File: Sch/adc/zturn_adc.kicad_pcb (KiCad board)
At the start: 4 copper layers, 86 x 75.8 mm, 115 parts, among them CN1 SMA, CN2 SMA, CN3 AudioJack, J1 JP2, J3 JP2, J4 JP2, P1 CONN_02X40, T1 ETC1-1-13, U1 LTC2292, U2 LP5907_SOT-23, U3 LP5907_SOT-23, U4 NC7SVU04-SC70, U5 NC7SVU04-SC70, U6 NAU8822LYG, X1 TCXO

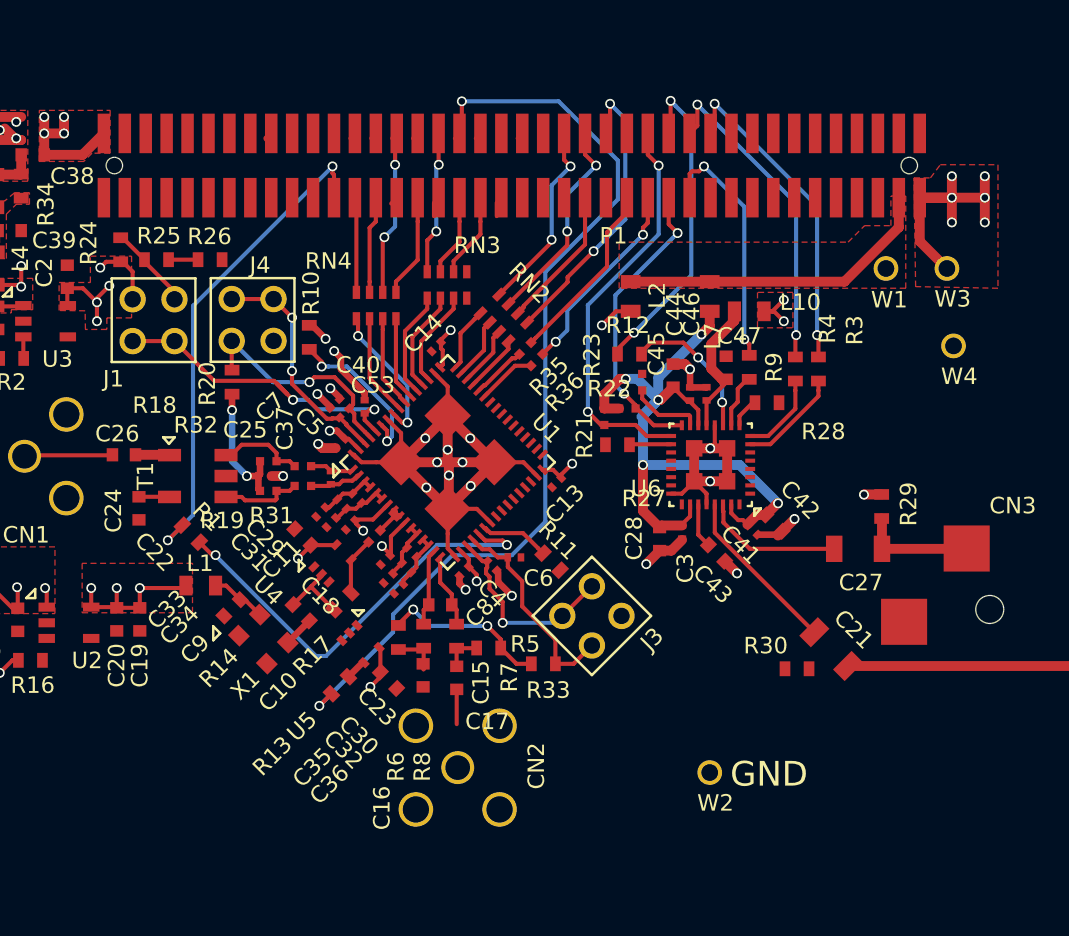
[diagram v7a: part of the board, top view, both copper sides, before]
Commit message: Removed unnecessary resistor array
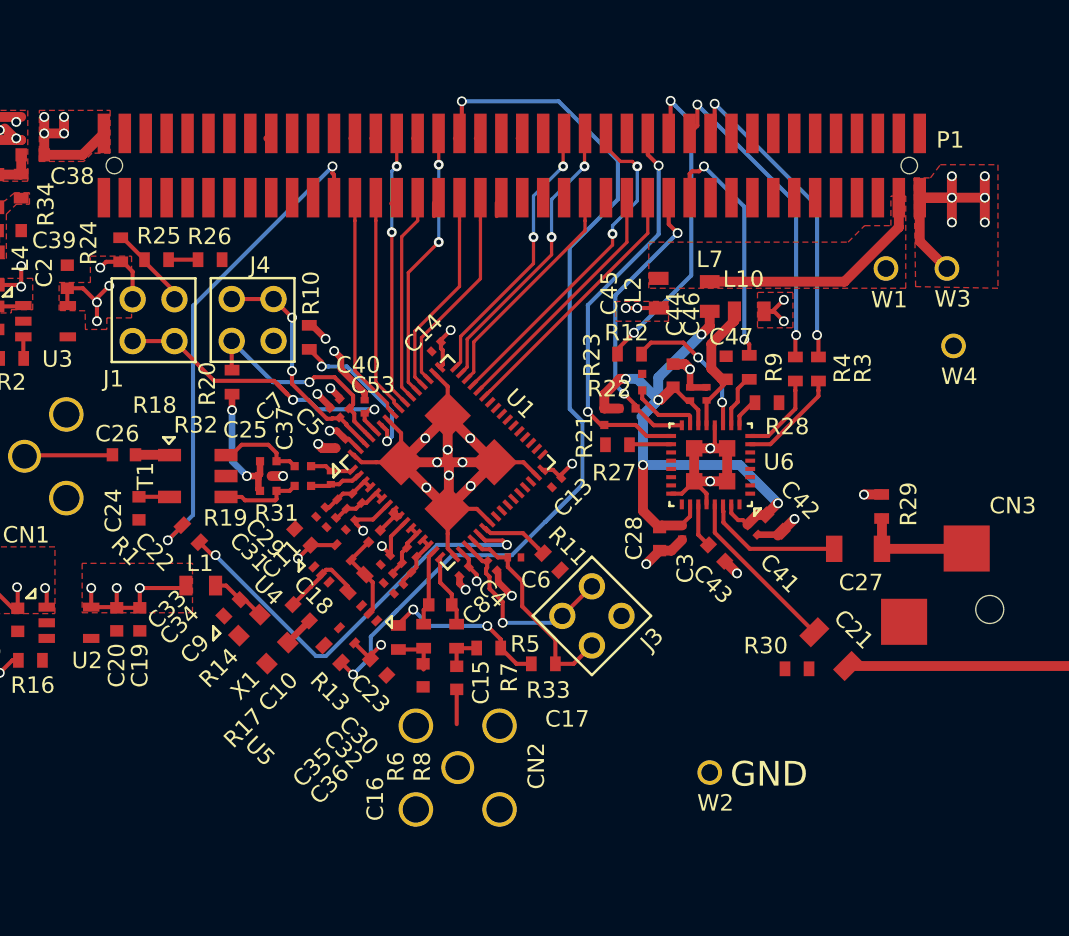
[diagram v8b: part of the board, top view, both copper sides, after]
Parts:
- removed R35, R36: 22, adc_lib:R0402
- removed RN2, RN3, RN4: 22, adc_lib:EXB-38V220JV
- moved R13 1.95 mm to (136.7, 108.0), turned to 135 degrees
- moved L2 1.71 mm to (156.5, 86.1)
- moved R17 1.39 mm to (138.2, 103.7)
- moved U5 1.21 mm to (138.2, 106.2), turned to 135 degrees
- moved C23 1.00 mm to (139.5, 108.8)
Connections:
- U1 pad 43: Net-(R36-Pad2) -> /CN/IO_B35_LP3
- U1 pad 44: Net-(R35-Pad2) -> /CN/IO_B35_LN3
- U1 pad 45: Net-(RN2-Pad4) -> /CN/IO_B35_LP6
- U1 pad 46: Net-(RN2-Pad3) -> /CN/IO_B35_LP5
- U1 pad 47: Net-(RN2-Pad2) -> /CN/IO_B35_LN6
- U1 pad 48: Net-(RN2-Pad1) -> /CN/IO_B35_LP8
- U1 pad 51: Net-(RN3-Pad3) -> /CN/IO_B35_LP9
- U1 pad 52: Net-(RN3-Pad2) -> /CN/IO_B35_LN9
- U1 pad 53: Net-(RN3-Pad1) -> /CN/IO_B35_LN12
- U1 pad 54: Net-(RN4-Pad4) -> /CN/IO_B35_LN11
- U1 pad 55: Net-(RN4-Pad3) -> /CN/IO_B35_LP14
- U1 pad 56: Net-(RN4-Pad2) -> /CN/IO_B35_LP13(MRCC)
- U1 pad 57: Net-(RN4-Pad1) -> /CN/IO_B35_LN13
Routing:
- net Net-(RN4-Pad1): track 8.65 -> 0.00 mm, vias 2 -> 0
- net /CN/IO_B35_LN13: track 5.79 -> 14.2 mm
- net /CN/IO_B35_LN12: track 8.69 -> 16.6 mm
- net /CN/IO_B35_LN9: track 5.80 -> 13.5 mm
- net /CN/IO_B35_LP9: track 5.22 -> 12.7 mm
- net /CN/IO_B35_LP13(MRCC): track 5.91 -> 13.4 mm
- net /CN/IO_B35_LP14: track 10.1 -> 16.9 mm
- net Net-(RN3-Pad1): track 6.47 -> 0.00 mm
- net /CN/IO_B35_LN11: track 6.30 -> 12.7 mm
- net Net-(RN3-Pad2): track 6.22 -> 0.00 mm
- net Net-(RN4-Pad2): track 6.17 -> 0.00 mm
- net /CN/IO_B35_LN3: track 11.2 -> 17.2 mm
- net Net-(RN3-Pad3): track 5.91 -> 0.00 mm
- net Net-(RN4-Pad3): track 5.64 -> 0.00 mm
- net /CN/IO_B35_LP5: track 9.02 -> 14.3 mm
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- added copper zone on F.Cu, net Net-(C13-Pad1)
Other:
- net class DOUT added: clearance 0.2, trace_width 0.2, via_dia 0.6, via_drill 0.3
- rule trace_min: 0.25 -> 0.2
